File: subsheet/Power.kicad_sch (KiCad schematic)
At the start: 26 parts, among them J501 DAISY_CHAIN, J502 PWR_IN, Q501 DTC114E, Q502 DTC114E, U501 TPS2552DBV, U502 TPS2552DBV

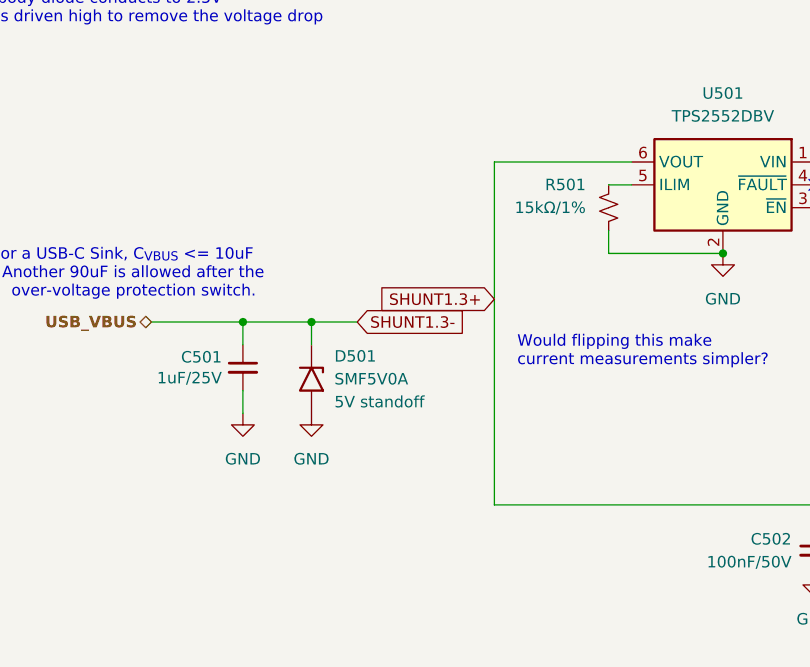
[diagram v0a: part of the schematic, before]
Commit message: PCB changes, added useful connectors
Added a whole bunch of things that should make it useful - e.g.
ethernet, an extra flash chip for general storage, piicodev connectors
for I2C.

Also added a GPIB connector footprint; dev-board version worked nicely,
but may as well make this work for that too. Saves bying dev boards : )
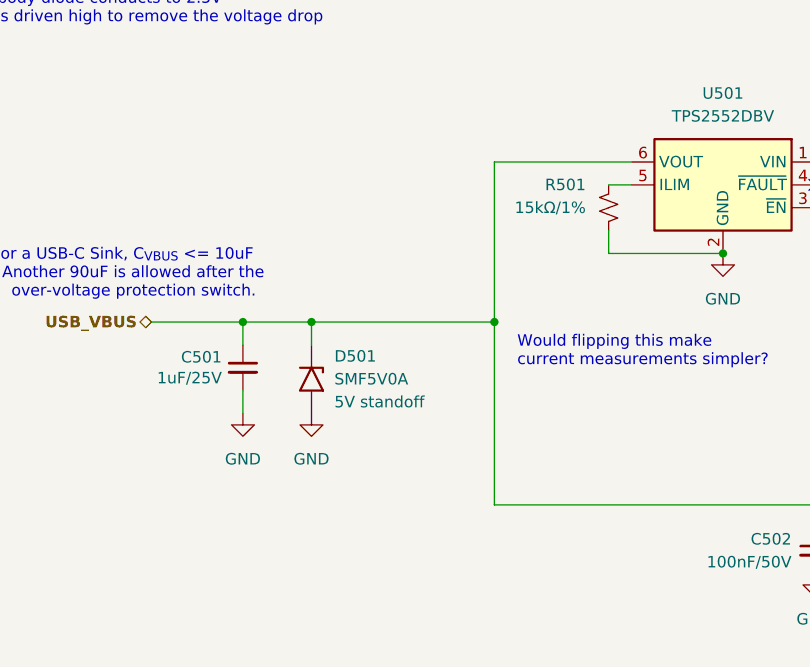
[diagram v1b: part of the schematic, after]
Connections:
- net SHUNT1.3- is gone; now on net USB_VBUS: C501.1, D501.1 (A1)
- net SHUNT1.3+ renamed USB_VBUS
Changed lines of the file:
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@@
+		(color 0 0 0 0)
+	)
+	(junction
+		(at 71.12 40.64)
+		(diameter 0)
 		(color 0 0 0 0)
 	)
@@
 	(wire
 		(pts
+			(xy 71.12 40.64) (xy 71.12 60.96)
+		)
+		(stroke
+			(width 0)
+			(type default)
+		)
+	)
+	(wire
+		(pts
 			(xy 33.02 121.92) (xy 48.26 121.92)
 		)
@@
 	(wire
 		(pts
-			(xy 50.8 40.64) (xy 55.88 40.64)
+			(xy 50.8 40.64) (xy 71.12 40.64)
 		)
 		(stroke
@@
 	(wire
 		(pts
-			(xy 71.12 22.86) (xy 71.12 60.96)
+			(xy 71.12 22.86) (xy 71.12 40.64)
 		)
 		(stroke
@@
 		)
 	)
-	(global_label "SHUNT1.3-"
-		(shape input)
-		(at 55.88 40.64 0)
-		(fields_autoplaced yes)
-		(effects
-			(font
-				(size 1.27 1.27)
-			)
-			(justify left)
-		)
-		(property "Intersheetrefs" "${INTERSHEET_REFS}"
-			(at 69.63 40.64 0)
-			(effects
-				(font
-					(size 1.27 1.27)
-				)
-				(justify left)
-				(hide yes)
-			)
-		)
-	)
 	(global_label "3v3_{LED}"
 		(shape input)
@@
 				(hide yes)
 			)
-		)
-	)
-	(global_label "SHUNT1.3+"
-		(shape input)
-		(at 71.12 38.1 180)
-		(fields_autoplaced yes)
-		(effects
-			(font
-				(size 1.27 1.27)
-			)
-			(justify right)
-		)
-		(property "Intersheetrefs" "${INTERSHEET_REFS}"
-			(at 57.37 38.1 0)
-			(effects
-				(font
-					(size 1.27 1.27)
-				)
-				(justify right)
-				(hide yes)
-			)

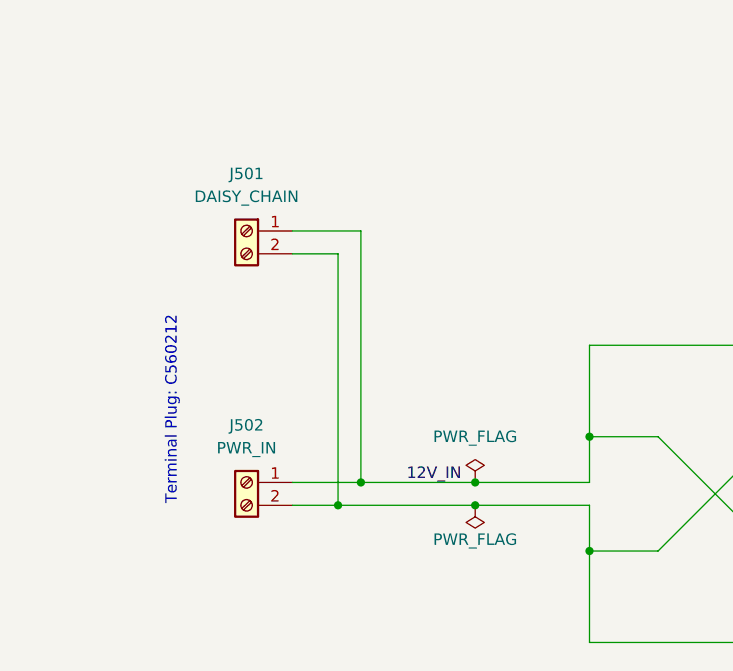
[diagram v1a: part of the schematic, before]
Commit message: Add barrel jack to schematic
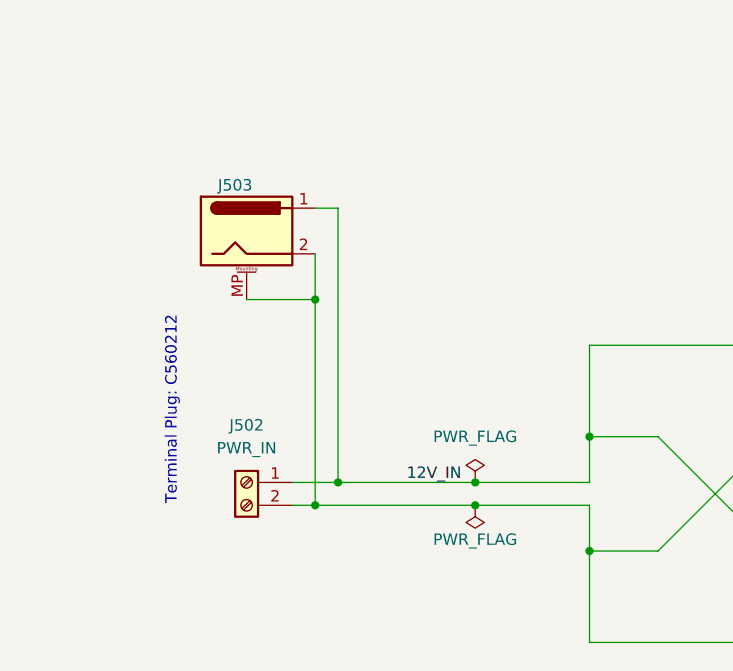
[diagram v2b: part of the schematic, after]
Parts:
- removed J501: DAISY_CHAIN, Connector_TerminalBlock_custom:Ningbo_Xinlaiya_XY2500R-D-5.08-2P_1x02_P5.08mm_Horizontal, symbol Connector:Screw_Terminal_01x02
- added J503: Barrel_Jack, Connector_BarrelJack:BarrelJack_CUI_PJ-063AH_Horizontal, symbol Connector:Barrel_Jack_MountingPin
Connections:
- net 12V_IN: now also J503.1
- net at D506.2 (A), D508.1 (K), J502.2 (Pin_2): now also J503.2, J503.MP (MountPin)
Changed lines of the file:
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@@
 	)
 	(junction
+		(at 30.48 99.06)
+		(diameter 0)
+		(color 0 0 0 0)
+	)
+	(junction
 		(at 220.98 119.38)
 		(diameter 0)
@@
 	)
 	(junction
-		(at 134.62 71.12)
+		(at 33.02 119.38)
 		(diameter 0)
 		(color 0 0 0 0)
 	)
 	(junction
-		(at 33.02 121.92)
+		(at 134.62 71.12)
 		(diameter 0)
 		(color 0 0 0 0)
@@
 	)
 	(junction
-		(at 35.56 119.38)
+		(at 30.48 121.92)
 		(diameter 0)
 		(color 0 0 0 0)
@@
 	(wire
 		(pts
-			(xy 33.02 121.92) (xy 48.26 121.92)
-		)
-		(stroke
-			(width 0)
-			(type default)
-		)
-	)
-	(wire
-		(pts
 			(xy 220.98 119.38) (xy 220.98 124.46)
 		)
@@
 	(wire
 		(pts
-			(xy 27.94 119.38) (xy 35.56 119.38)
+			(xy 33.02 119.38) (xy 48.26 119.38)
 		)
 		(stroke
@@
 	(wire
 		(pts
-			(xy 106.68 22.86) (xy 119.38 22.86)
+			(xy 30.48 93.98) (xy 30.48 99.06)
 		)
 		(stroke
@@
 	(wire
 		(pts
-			(xy 83.82 33.02) (xy 96.52 33.02)
+			(xy 106.68 22.86) (xy 119.38 22.86)
 		)
 		(stroke
@@
 	(wire
 		(pts
-			(xy 96.52 121.92) (xy 111.76 121.92)
+			(xy 83.82 33.02) (xy 96.52 33.02)
 		)
 		(stroke
@@
 	(wire
 		(pts
-			(xy 43.18 43.18) (xy 43.18 40.64)
+			(xy 96.52 121.92) (xy 111.76 121.92)
 		)
 		(stroke
@@
 	(wire
 		(pts
-			(xy 60.96 104.14) (xy 60.96 114.3)
+			(xy 43.18 43.18) (xy 43.18 40.64)
 		)
 		(stroke
@@
 	(wire
 		(pts
-			(xy 220.98 43.18) (xy 190.5 43.18)
+			(xy 60.96 104.14) (xy 60.96 114.3)
 		)
 		(stroke
@@
 	(wire
 		(pts
-			(xy 35.56 91.44) (xy 35.56 119.38)
+			(xy 220.98 43.18) (xy 190.5 43.18)
 		)
 		(stroke
@@
 	(wire
 		(pts
-			(xy 27.94 93.98) (xy 33.02 93.98)
-		)
-		(stroke
-			(width 0)
-			(type default)
-		)
-	)
-	(wire
-		(pts
 			(xy 106.68 175.26) (xy 109.22 175.26)
 		)
@@
 	(wire
 		(pts
-			(xy 33.02 121.92) (xy 27.94 121.92)
+			(xy 27.94 121.92) (xy 30.48 121.92)
 		)
 		(stroke
@@
 	(wire
 		(pts
+			(xy 30.48 88.9) (xy 33.02 88.9)
+		)
+		(stroke
+			(width 0)
+			(type default)
+		)
+	)
+	(wire
+		(pts
 			(xy 119.38 30.48) (xy 109.22 30.48)
 		)
@@
 	(wire
 		(pts
+			(xy 30.48 121.92) (xy 48.26 121.92)
+		)
+		(stroke
+			(width 0)
+			(type default)
+		)
+	)
+	(wire
+		(pts
 			(xy 124.46 25.4) (xy 124.46 22.86)
 		)
@@
 	(wire
 		(pts
+			(xy 33.02 88.9) (xy 33.02 119.38)
+		)
+		(stroke
+			(width 0)
+			(type default)
+		)
+	)
+	(wire
+		(pts
 			(xy 220.98 33.02) (xy 220.98 35.56)
 		)
@@
 	(wire
 		(pts
-			(xy 33.02 93.98) (xy 33.02 121.92)
-		)
-		(stroke
-			(width 0)
-			(type default)
-		)
-	)
-	(wire
-		(pts
 			(xy 43.18 50.8) (xy 43.18 48.26)
 		)
@@
 	(wire
 		(pts
-			(xy 27.94 91.44) (xy 35.56 91.44)
-		)
-		(stroke
-			(width 0)
-			(type default)
-		)
-	)
-	(wire
-		(pts
 			(xy 190.5 39.37) (xy 190.5 43.18)
 		)
@@
 	(wire
 		(pts
-			(xy 35.56 119.38) (xy 48.26 119.38)
+			(xy 27.94 119.38) (xy 33.02 119.38)
 		)
 		(stroke
@@
 	(wire
 		(pts
+			(xy 22.86 99.06) (xy 30.48 99.06)
+		)
+		(stroke
+			(width 0)
+			(type default)
+		)
+	)
+	(wire
+		(pts
+			(xy 30.48 99.06) (xy 30.48 121.92)
+		)
+		(stroke
+			(width 0)
+			(type default)
+		)
+	)
+	(wire
+		(pts
 			(xy 220.98 43.18) (xy 254 43.18)
 		)
@@
 	)
 	(symbol
+		(lib_id "Connector:Barrel_Jack_MountingPin")
+		(at 22.86 91.44 0)
+		(unit 1)
+		(exclude_from_sim no)
+		(in_bom yes)
+		(on_board yes)
+		(dnp no)
+		(property "Reference" "J503"
+			(at 21.59 86.36 0)
+			(effects
+				(font
+					(size 1.27 1.27)
+				)
+			)
+		)
+		(property "Value" "Barrel_Jack"
+			(at 24.3078 85.6996 0)
+			(effects
+				(font
+					(size 1.27 1.27)
+				)
+				(hide yes)
+			)
+		)
+		(property "Footprint" "Connector_BarrelJack:BarrelJack_CUI_PJ-063AH_Horizontal"
+			(at 24.13 92.456 0)
+			(effects
+				(font
+					(size 1.27 1.27)
+				)
+				(hide yes)
+			)
+		)
+		(property "Datasheet" "~"
+			(at 24.13 92.456 0)
+			(effects
+				(font
+					(size 1.27 1.27)
+				)
+				(hide yes)
+			)
+		)
+		(property "Description" ""
+			(at 22.86 91.44 0)
+			(effects
+				(font
+					(size 1.27 1.27)
+				)
+				(hide yes)
+			)
+		)
+		(pin "1"
+		)
+		(pin "2"
+		)
+		(pin "MP"
+		)
+		(instances
+			(project "ESP_bare_chip_test_board"
+				(path "/45b6f84a-e69b-48be-a49b-bc68872e2c15/28425a28-8968-4679-b18b-58814452f93f"
+					(reference "J503")
+					(unit 1)
+				)
+			)
+		)
+	)
+	(symbol
 		(lib_id "power:+3V3")
 		(at 259.08 147.32 270)
@@
 					(unit 1)
 				)
-			)
-		)
-	)
-	(symbol
-		(lib_id "Connector:Screw_Terminal_01x02")
-		(at 22.86 91.44 0)
-		(mirror y)
-		(unit 1)
-		(exclude_from_sim no)
-		(in_bom yes)
-		(on_board yes)
-		(dnp no)
-		(fields_autoplaced yes)
-		(property "Reference" "J501"
-			(at 22.86 85.09 0)
-			(effects
-				(font
-					(size 1.27 1.27)
-				)
-			)
-		)
-		(property "Value" "DAISY_CHAIN"
-			(at 22.86 87.63 0)
-			(effects
-				(font
-					(size 1.27 1.27)
-				)
-			)
-		)
-		(property "Footprint" "Connector_TerminalBlock_custom:Ningbo_Xinlaiya_XY2500R-D-5.08-2P_1x02_P5.08mm_Horizontal"
-			(at 22.86 91.44 0)
-			(effects
-				(font
-					(size 1.27 1.27)
-				)
-				(hide yes)
-			)
-		)
-		(property "Datasheet" "~"
-			(at 22.86 91.44 0)
-			(effects
-				(font
-					(size 1.27 1.27)
-				)
-				(hide yes)
-			)
-		)
-		(property "Description" ""
-			(at 22.86 91.44 0)
-			(effects
-				(font
-					(size 1.27 1.27)
-				)
-				(hide yes)
-			)
-		)
-		(property "LCSC" "C505824"
-			(at 22.86 91.44 0)
-			(effects
-				(font
-					(size 1.27 1.27)
-				)
-				(hide yes)
-			)
-		)
-		(property "JLCPCB_IGNORE" ""
-			(at 22.86 91.44 0)
-			(effects
-				(font
-					(size 1.27 1.27)
-				)
-				(hide yes)
-			)
-		)
-		(property "Comment" "Through-hole"
-			(at 22.86 91.44 0)
-			(effects
-				(font
-					(size 1.27 1.27)
-				)
-				(hide yes)
-			)
-		)
-		(property "JLCPCB_CORRECTION" "2.54;0;0"
-			(at 22.86 91.44 0)
-			(effects
-				(font
-					(size 1.27 1.27)
-				)
-				(hide yes)
-			)
-		)
-		(pin "1"
-		)
-		(pin "2"
-		)
-		(instances
-			(project "ESP_bare_chip_test_board"
-				(path "/45b6f84a-e69b-48be-a49b-bc68872e2c15/28425a28-8968-4679-b18b-58814452f93f"
-					(reference "J501")
-					(unit 1)
-				)

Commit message: Uknown changes?File formats?
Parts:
- renumbered D505 to D502, D506 to D503, D507 to D504, D508 to D505, D503 to D506, D504 to D507, D502 to D508, J503 to J501, R508 to R503, R503 to R504, R504 to R505, R509 to R506, R505 to R507, R506 to R508, R507 to R509

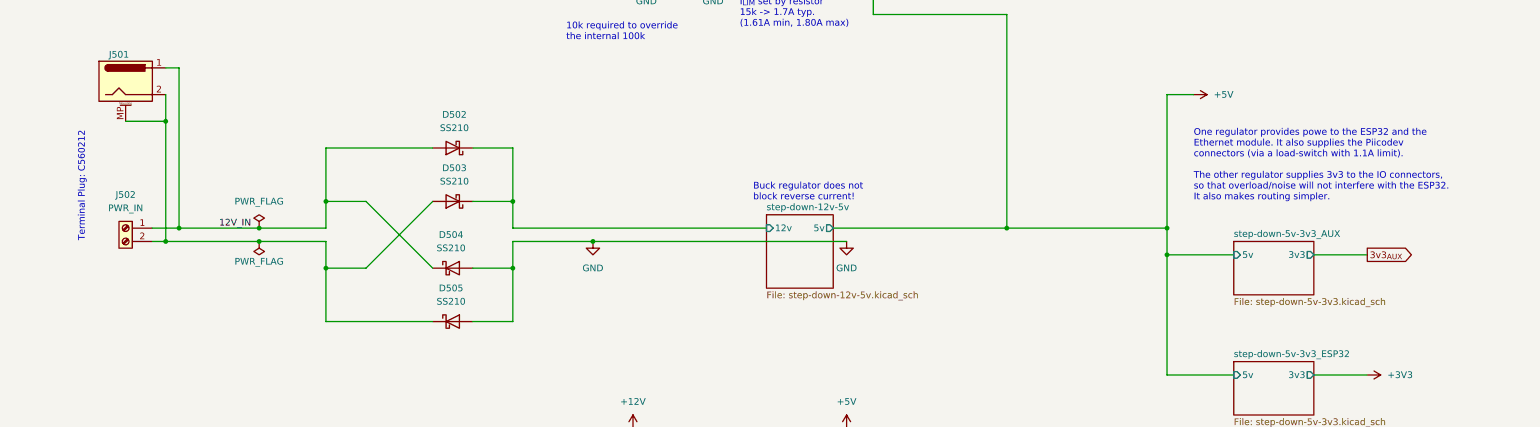
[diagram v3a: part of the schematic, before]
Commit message: Unknown changes? Arranging components, I believe
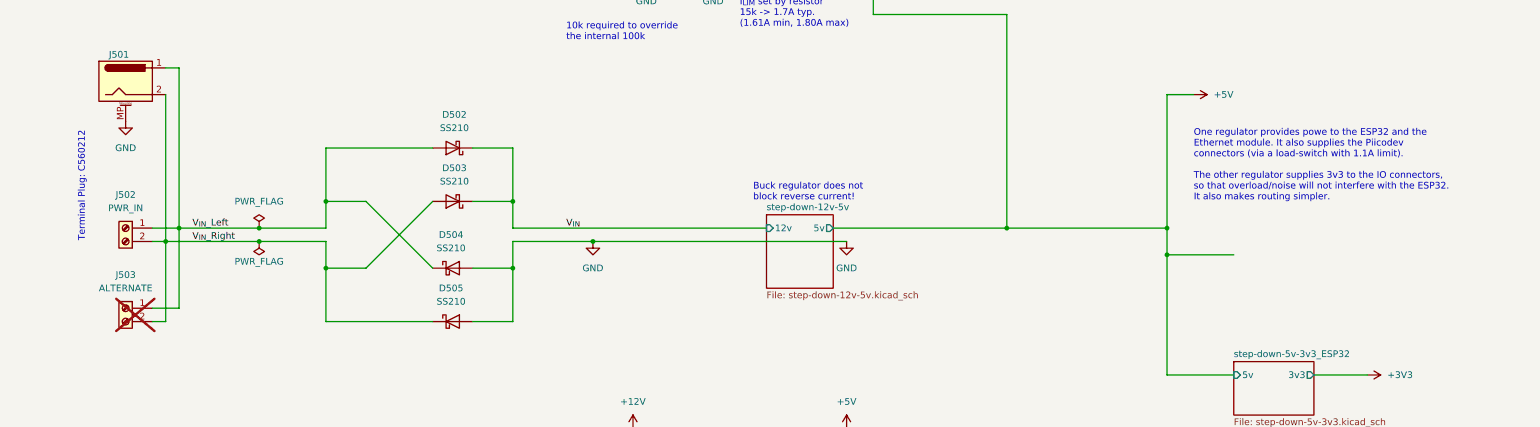
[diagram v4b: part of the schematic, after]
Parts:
- added J503: ALTERNATE, Connector_TerminalBlock_custom:Ningbo_Xinlaiya_XY2500R-D-5.08-2P_1x02_P5.08mm_Horizontal, symbol Connector:Screw_Terminal_01x02
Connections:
- net GND: now also J501.MP (MountPin)
- net V_{IN}_Right: now reaches D503.2 (A), D505.1 (K), J501.2, J502.2 (Pin_2)
- net V_{IN}_Right: now also J503.2 (Pin_2); no longer J501.MP (MountPin)
- net 12V_IN renamed V_{IN}_Left
- net V_{IN}_Left: now also J503.1 (Pin_1)
- net step-down-12v-5v/12v renamed V_{IN}
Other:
- removed sheet step-down-5v-3v3_AUX
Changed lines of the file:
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@@
 	)
 	(junction
-		(at 30.48 99.06)
-		(diameter 0)
-		(color 0 0 0 0)
-	)
-	(junction
 		(at 220.98 119.38)
 		(diameter 0)
@@
 	(wire
 		(pts
-			(xy 30.48 93.98) (xy 30.48 99.06)
-		)
-		(stroke
-			(width 0)
-			(type default)
-		)
-	)
-	(wire
-		(pts
 			(xy 106.68 22.86) (xy 119.38 22.86)
 		)
@@
 	(wire
 		(pts
+			(xy 30.48 137.16) (xy 30.48 121.92)
+		)
+		(stroke
+			(width 0)
+			(type default)
+		)
+	)
+	(wire
+		(pts
 			(xy 119.38 172.72) (xy 119.38 177.8)
 		)
@@
 	(wire
 		(pts
+			(xy 27.94 134.62) (xy 33.02 134.62)
+		)
+		(stroke
+			(width 0)
+			(type default)
+		)
+	)
+	(wire
+		(pts
 			(xy 149.86 182.88) (xy 151.13 182.88)
 		)
@@
 	(wire
 		(pts
+			(xy 27.94 137.16) (xy 30.48 137.16)
+		)
+		(stroke
+			(width 0)
+			(type default)
+		)
+	)
+	(wire
+		(pts
 			(xy 30.48 121.92) (xy 48.26 121.92)
 		)
@@
 	(wire
 		(pts
-			(xy 248.92 124.46) (xy 259.08 124.46)
-		)
-		(stroke
-			(width 0)
-			(type default)
-		)
-	)
-	(wire
-		(pts
 			(xy 241.3 33.02) (xy 241.3 35.56)
 		)
@@
 	(wire
 		(pts
-			(xy 248.92 147.32) (xy 259.08 147.32)
+			(xy 33.02 134.62) (xy 33.02 119.38)
 		)
 		(stroke
@@
 	(wire
 		(pts
-			(xy 241.3 40.64) (xy 241.3 50.8)
+			(xy 248.92 147.32) (xy 259.08 147.32)
 		)
 		(stroke
@@
 	(wire
 		(pts
-			(xy 220.98 124.46) (xy 220.98 147.32)
+			(xy 241.3 40.64) (xy 241.3 50.8)
 		)
 		(stroke
@@
 	(wire
 		(pts
-			(xy 220.98 93.98) (xy 220.98 119.38)
+			(xy 220.98 124.46) (xy 220.98 147.32)
 		)
 		(stroke
@@
 	(wire
 		(pts
-			(xy 22.86 99.06) (xy 30.48 99.06)
+			(xy 220.98 93.98) (xy 220.98 119.38)
 		)
 		(stroke
@@
 	(wire
 		(pts
-			(xy 30.48 99.06) (xy 30.48 121.92)
+			(xy 30.48 93.98) (xy 30.48 121.92)
 		)
 		(stroke
@@
 		)
 	)
+	(label "V_{IN}"
+		(at 106.68 119.38 0)
+		(fields_autoplaced yes)
+		(effects
+			(font
+				(size 1.27 1.27)
+			)
+			(justify left bottom)
+		)
+	)
 	(label "~{SINK_EN}"
 		(at 109.22 50.8 0)
@@
 		)
 	)
-	(label "12V_IN"
-		(at 40.64 119.38 0)
+	(label "V_{IN}_Left"
+		(at 35.56 119.38 0)
+		(fields_autoplaced yes)
+		(effects
+			(font
+				(size 1.27 1.27)
+			)
+			(justify left bottom)
+		)
+	)
+	(label "V_{IN}_Right"
+		(at 35.56 121.92 0)
 		(fields_autoplaced yes)
 		(effects
@@
 		)
 	)
-	(global_label "3v3_{AUX}"
-		(shape output)
-		(at 259.08 124.46 0)
-		(fields_autoplaced yes)
-		(effects
-			(font
-				(size 1.27 1.27)
-			)
-			(justify left)
-		)
-		(property "Intersheetrefs" "${INTERSHEET_REFS}"
-			(at 268.4055 124.46 0)
-			(effects
-				(font
-					(size 1.27 1.27)
-				)
-				(justify left)
-				(hide yes)
-			)
-		)
-	)
 	(global_label "+12V"
 		(shape input)
@@
 	)
 	(symbol
+		(lib_id "Connector:Screw_Terminal_01x02")
+		(at 22.86 134.62 0)
+		(mirror y)
+		(unit 1)
+		(exclude_from_sim yes)
+		(in_bom no)
+		(on_board yes)
+		(dnp yes)
+		(fields_autoplaced yes)
+		(property "Reference" "J503"
+			(at 22.86 128.27 0)
+			(effects
+				(font
+					(size 1.27 1.27)
+				)
+			)
+		)
+		(property "Value" "ALTERNATE"
+			(at 22.86 130.81 0)
+			(effects
+				(font
+					(size 1.27 1.27)
+				)
+			)
+		)
+		(property "Footprint" "Connector_TerminalBlock_custom:Ningbo_Xinlaiya_XY2500R-D-5.08-2P_1x02_P5.08mm_Horizontal"
+			(at 22.86 134.62 0)
+			(effects
+				(font
+					(size 1.27 1.27)
+				)
+				(hide yes)
+			)
+		)
+		(property "Datasheet" "~"
+			(at 22.86 134.62 0)
+			(effects
+				(font
+					(size 1.27 1.27)
+				)
+				(hide yes)
+			)
+		)
+		(property "Description" ""
+			(at 22.86 134.62 0)
+			(effects
+				(font
+					(size 1.27 1.27)
+				)
+				(hide yes)
+			)
+		)
+		(property "LCSC" "C505824"
+			(at 22.86 134.62 0)
+			(effects
+				(font
+					(size 1.27 1.27)
+				)
+				(hide yes)
+			)
+		)
+		(property "JLCPCB_IGNORE" ""
+			(at 22.86 134.62 0)
+			(effects
+				(font
+					(size 1.27 1.27)
+				)
+				(hide yes)
+			)
+		)
+		(property "Comment" "Through-hole"
+			(at 22.86 134.62 0)
+			(effects
+				(font
+					(size 1.27 1.27)
+				)
+				(hide yes)
+			)
+		)
+		(property "JLCPCB_CORRECTION" "2.54;0;0"
+			(at 22.86 134.62 0)
+			(effects
+				(font
+					(size 1.27 1.27)
+				)
+				(hide yes)
+			)
+		)
+		(pin "1"
+		)
+		(pin "2"
+		)
+		(instances
+			(project "ESP_bare_chip_test_board"
+				(path "/45b6f84a-e69b-48be-a49b-bc68872e2c15/28425a28-8968-4679-b18b-58814452f93f"
+					(reference "J503")
+					(unit 1)
+				)
+			)
+		)
+	)
+	(symbol
 		(lib_id "power:GND")
 		(at 43.18 50.8 0)
@@
 	(symbol
 		(lib_id "power:GND")
+		(at 22.86 99.06 0)
+		(unit 1)
+		(exclude_from_sim no)
+		(in_bom yes)
+		(on_board yes)
+		(dnp no)
+		(fields_autoplaced yes)
+		(property "Reference" "#PWR0520"
+			(at 22.86 105.41 0)
+			(effects
+				(font
+					(size 1.27 1.27)
+				)
+				(hide yes)
+			)
+		)
+		(property "Value" "GND"
+			(at 22.86 104.14 0)
+			(effects
+				(font
+					(size 1.27 1.27)
+				)
+			)
+		)
+		(property "Footprint" ""
+			(at 22.86 99.06 0)
+			(effects
+				(font
+					(size 1.27 1.27)
+				)
+				(hide yes)
+			)
+		)
+		(property "Datasheet" ""
+			(at 22.86 99.06 0)
+			(effects
+				(font
+					(size 1.27 1.27)
+				)
+				(hide yes)
+			)
+		)
+		(property "Description" "Power symbol creates a global label with name \"GND\" , ground"
+			(at 22.86 99.06 0)
+			(effects
+				(font
+					(size 1.27 1.27)
+				)
+				(hide yes)
+			)
+		)
+		(pin "1"
+		)
+		(instances
+			(project "ESP_bare_chip_test_board"
+				(path "/45b6f84a-e69b-48be-a49b-bc68872e2c15/28425a28-8968-4679-b18b-58814452f93f"
+					(reference "#PWR0520")
+					(unit 1)
+				)
+			)
+		)
+	)
+	(symbol
+		(lib_id "power:GND")
 		(at 111.76 121.92 0)
 		(unit 1)
@@
 				)
 			)
-		)
-	)
-	(sheet
-		(at 233.68 121.92)
-		(size 15.24 10.16)
-		(fields_autoplaced yes)
-		(stroke
-			(width 0.1524)
-			(type solid)
-		)
-		(fill
-			(color 255 229 191 1.0000)
-		)
-		(property "Sheetname" "step-down-5v-3v3_AUX"
-			(at 233.68 121.2084 0)
-			(effects
-				(font
-					(size 1.27 1.27)
-				)
-				(justify left bottom)
-			)
-		)
-		(property "Sheetfile" "step-down-5v-3v3.kicad_sch"
-			(at 233.68 132.6646 0)
-			(effects
-				(font
-					(size 1.27 1.27)
-				)
-				(justify left top)
-			)
-		)
-		(pin "5v" input
-			(at 233.68 124.46 180)
-			(effects
-				(font
-					(size 1.27 1.27)
-				)
-				(justify left)
-			)
-		)
-		(pin "3v3" output
-			(at 248.92 124.46 0)
-			(effects
-				(font
-					(size 1.27 1.27)
-				)
-				(justify right)
-			)
-		)
-		(instances
-			(project "ESP_bare_chip_test_board"
-				(path "/45b6f84a-e69b-48be-a49b-bc68872e2c15/28425a28-8968-4679-b18b-58814452f93f"
-					(page "9")
-				)
-			)
